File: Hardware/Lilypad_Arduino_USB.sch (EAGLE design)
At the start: 44 parts, among them U1 MCP73831, U2 MIC5219, U3 ATMEGA32U4QFN, X1 USB-MICROB, Y1 8MHz

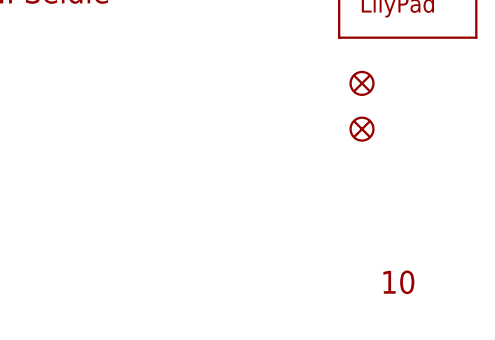
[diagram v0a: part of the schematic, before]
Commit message: Change micro USB connector to more robust package.
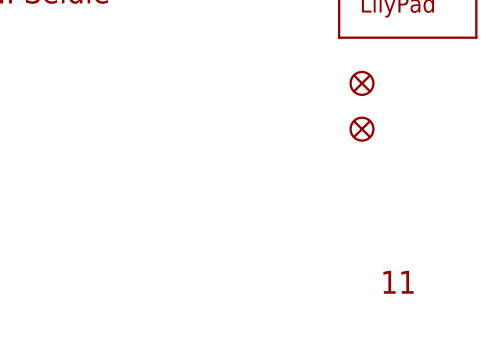
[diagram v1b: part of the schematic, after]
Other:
- note added: "11"
- note removed: "10"
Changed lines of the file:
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@@
 <layer number="144" name="Drill_legend" color="7" fill="1" visible="yes" active="yes"/>
 <layer number="151" name="HeatSink" color="7" fill="1" visible="yes" active="yes"/>
+<layer number="199" name="Contour" color="7" fill="1" visible="yes" active="yes"/>
 <layer number="200" name="200bmp" color="1" fill="10" visible="no" active="no"/>
 <layer number="201" name="201bmp" color="2" fill="1" visible="no" active="no"/>
@@
 <text x="45.72" y="120.65" size="1.27" layer="97">MIC5219 BYPASS</text>
 <text x="171.45" y="11.43" size="2.54" layer="94">Mike Hord</text>
-<text x="238.252" y="7.112" size="2.54" layer="94">10</text>
+<text x="238.252" y="7.112" size="2.54" layer="94">11</text>
 <text x="170.18" y="43.18" size="2.54" layer="94">Original Lilypad Design by:</text>
 <text x="170.18" y="39.37" size="2.54" layer="94">L. Buechly and N. Seidle</text>

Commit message: Changed version number in both files.
Masked via at .35, .275 to provide a test point for the charge circuit.
Add USR mask on the user control LED to make it more clear what it does.

Closes issues 1 and 2.
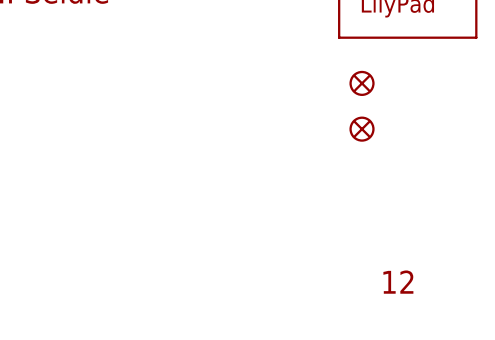
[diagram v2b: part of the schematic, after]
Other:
- note added: "12"
- note removed: "11"
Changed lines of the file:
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@@
 <text x="45.72" y="120.65" size="1.27" layer="97">MIC5219 BYPASS</text>
 <text x="171.45" y="11.43" size="2.54" layer="94">Mike Hord</text>
-<text x="238.252" y="7.112" size="2.54" layer="94">11</text>
+<text x="238.252" y="7.112" size="2.54" layer="94">12</text>
 <text x="170.18" y="43.18" size="2.54" layer="94">Original Lilypad Design by:</text>
 <text x="170.18" y="39.37" size="2.54" layer="94">L. Buechly and N. Seidle</text>

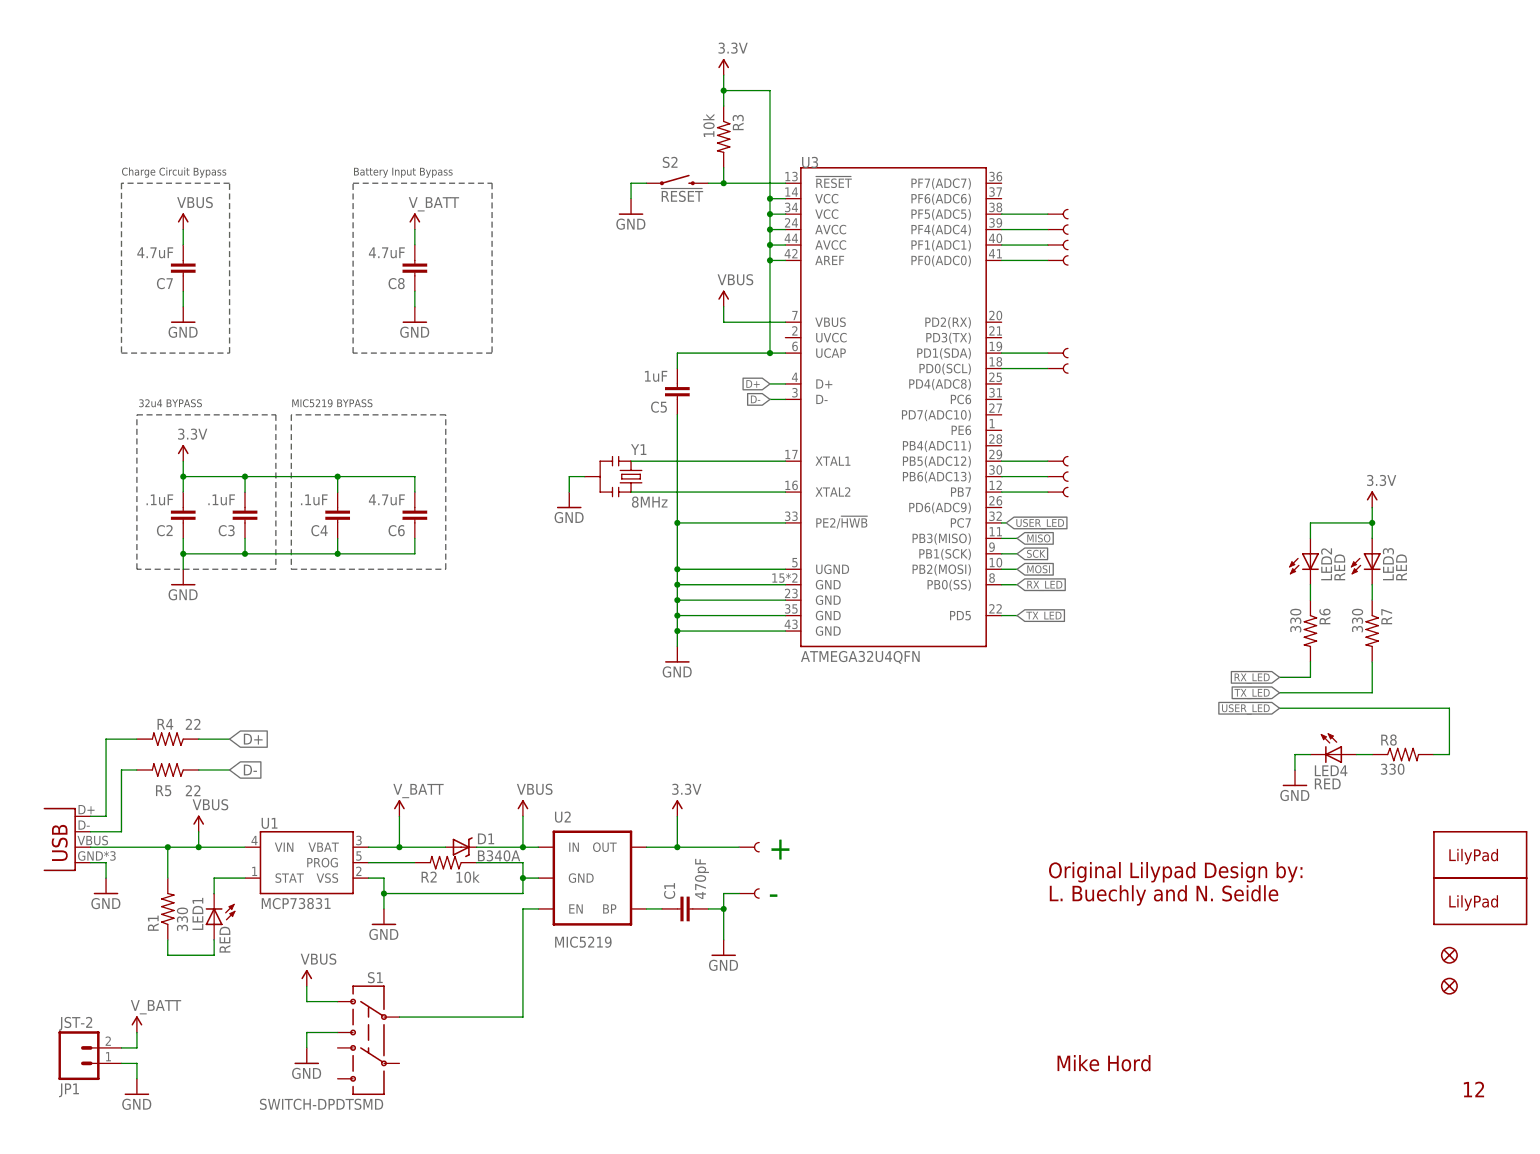
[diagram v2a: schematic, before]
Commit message: Quality Control Revision to PCB layout
Changed:
- Updated all 0402 footprints to 0603
- Updated with new 1:1 footprint of 32u4 IC
- Rerouted all traces straight away from IC
- Added trestrict under IC to mitigate gnd plane
- Moved crystal closer to IC
- Updated microUSB footprint for new production part
- Added test point for charge circuit
- Updated version number in bottom copper and schematic
- Added silk for charge and stat LEDs
- Added gnd vias to mitigate orphaned pours
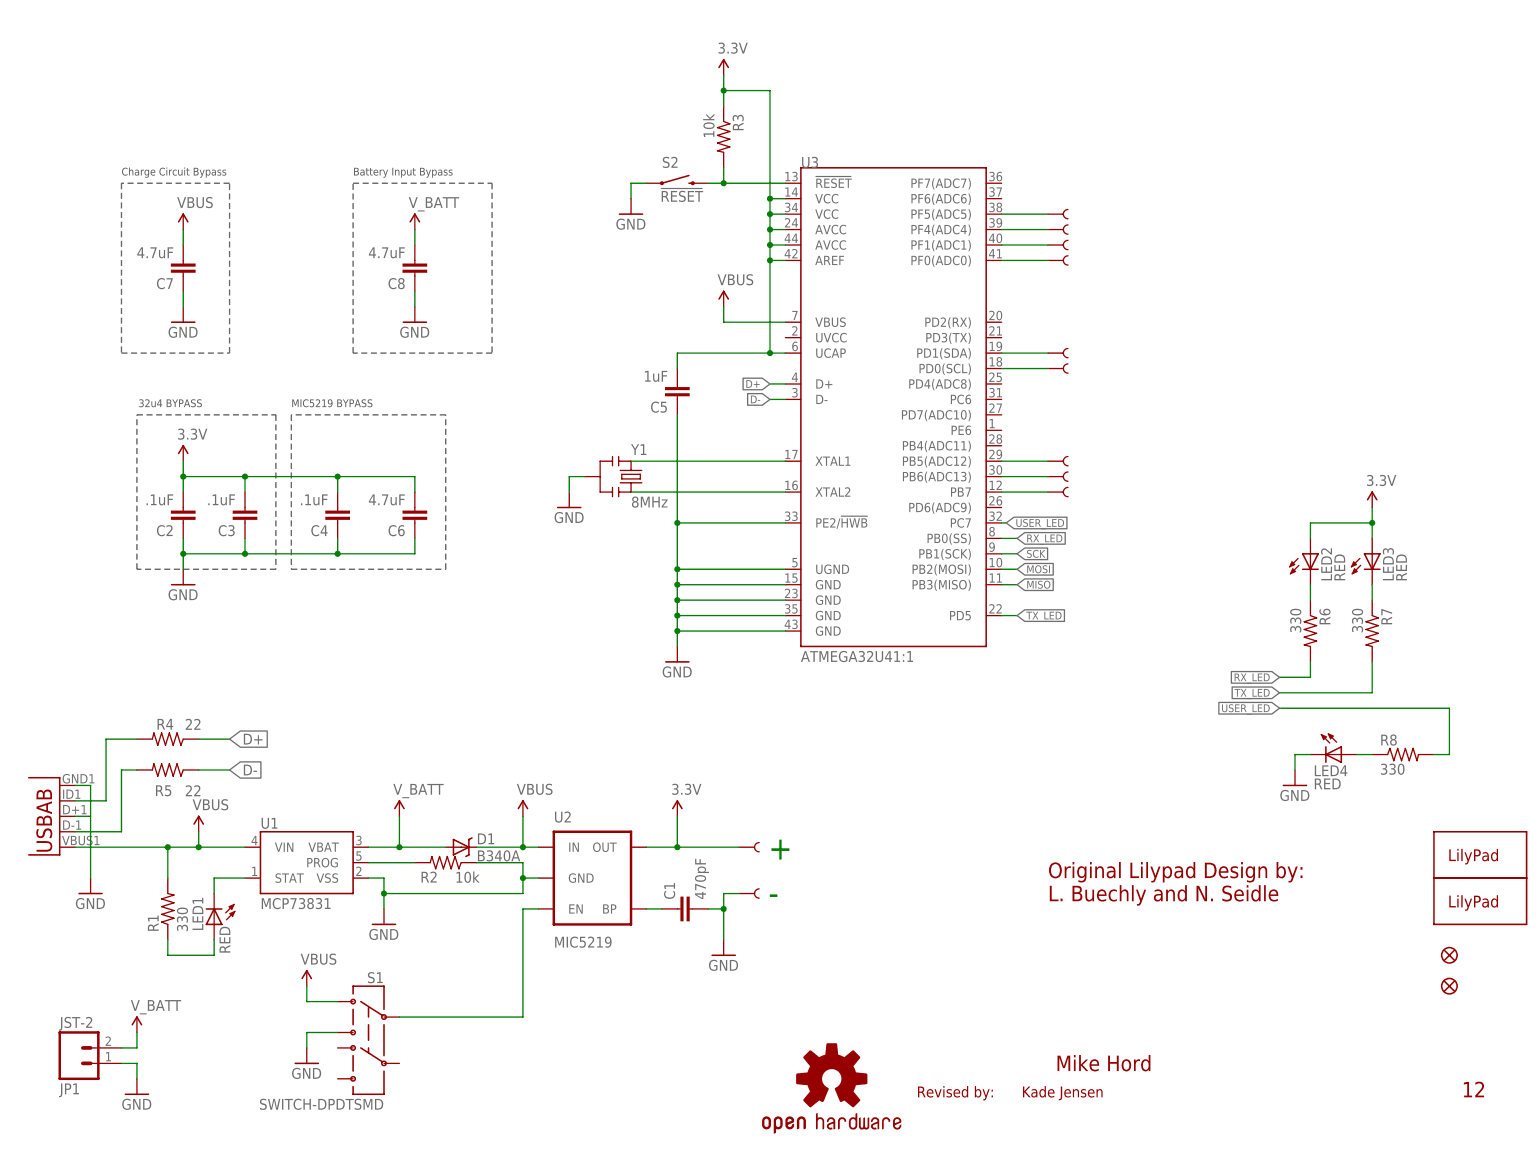
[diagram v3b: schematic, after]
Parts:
- added U$5: OSHW-LOGOM, SparkFun:OSHW-LOGOM
- JP2, JP3: value FIDUCIALUFIDUCIAL -> FIDUCIAL1X2; device SparkFun:FIDUCIALUFIDUCIAL -> SparkFun:FIDUCIAL1X2
- R2, R3, R4, R5, R6: device SparkFun-Passives:RESISTOR0603-RES -> SparkFun-Resistors:RESISTOR0603-RES
- U3: value ATMEGA32U4QFN -> ATMEGA32U41:1; device SparkFun-DigitalIC:ATMEGA32U4QFN -> Testing:ATMEGA32U41:1
- X1: value USB-MICROB -> (none); device SparkFun-Connectors:USB-MICROB -> Testing:USB-AB"""; PROD_ID CONN-09505 -> (none)
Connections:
- new net N$22: X1.D+
- net N$20: now also X1.USBID; no longer X1.D+
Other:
- note added: "Kade Jensen"
- note added: "Revised by:"
- moved on the sheet: U3
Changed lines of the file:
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@@
 <?xml version="1.0" encoding="utf-8"?>
 <!DOCTYPE eagle SYSTEM "eagle.dtd">
-<eagle version="6.3">
+<eagle version="6.4">
 <drawing>
 <settings>
@@
 <layer number="106" name="bPlate" color="7" fill="1" visible="yes" active="yes"/>
 <layer number="107" name="Crop" color="7" fill="1" visible="yes" active="yes"/>
+<layer number="108" name="tplace-old" color="10" fill="1" visible="yes" active="yes"/>
+<layer number="109" name="ref-old" color="11" fill="1" visible="yes" active="yes"/>
 <layer number="116" name="Patch_BOT" color="9" fill="4" visible="yes" active="yes"/>
 <layer number="121" name="_tsilk" color="7" fill="1" visible="yes" active="yes"/>
@@
 <attribute name="NO_PART" value="1"/>
 </part>
-<part name="U3" library="SparkFun-DigitalIC" deviceset="ATMEGA32U4" device="QFN">
+<part name="U3" library="Testing" deviceset="ATMEGA32U4" device="1:1">
 <attribute name="PROD_ID" value="IC-10828"/>
 </part>
@@
 <attribute name="PROD_ID" value="CONN-08352"/>
 </part>
-<part name="X1" library="SparkFun-Connectors" deviceset="USB" device="-MICROB">
-<attribute name="PROD_ID" value="CONN-09505"/>
-</part>
+<part name="X1" library="Testing" deviceset="USB-AB" device="&quot;&quot;&quot;"/>
 <part name="LED1" library="SparkFun-LED" deviceset="LED" device="0603" value="RED">
 <attribute name="PROD_ID" value="DIO-00819"/>
@@
 <part name="P+1" library="SparkFun-Aesthetics" deviceset="3.3V" device=""/>
 <part name="U$14" library="SparkFun-Aesthetics" deviceset="V_BATT" device=""/>
-<part name="R2" library="SparkFun-Passives" deviceset="RESISTOR" device="0603-RES" value="10k">
+<part name="R2" library="SparkFun-Resistors" deviceset="RESISTOR" device="0603-RES" value="10k">
 <attribute name="PROD_ID" value="RES-00824"/>
 </part>
 <part name="GND4" library="SparkFun-Aesthetics" deviceset="GND" device=""/>
 <part name="P+2" library="SparkFun-Aesthetics" deviceset="3.3V" device=""/>
-<part name="R3" library="SparkFun-Passives" deviceset="RESISTOR" device="0603-RES" value="10k">
+<part name="R3" library="SparkFun-Resistors" deviceset="RESISTOR" device="0603-RES" value="10k">
 <attribute name="PROD_ID" value="RES-00824"/>
 </part>
 <part name="GND5" library="SparkFun-Aesthetics" deviceset="GND" device=""/>
 <part name="U$16" library="SparkFun-Aesthetics" deviceset="5V" device="" value="VBUS"/>
-<part name="R4" library="SparkFun-Passives" deviceset="RESISTOR" device="0603-RES" value="22">
+<part name="R4" library="SparkFun-Resistors" deviceset="RESISTOR" device="0603-RES" value="22">
 <attribute name="PROD_ID" value="RES-08698"/>
 </part>
-<part name="R5" library="SparkFun-Passives" deviceset="RESISTOR" device="0603-RES" value="22">
+<part name="R5" library="SparkFun-Resistors" deviceset="RESISTOR" device="0603-RES" value="22">
 <attribute name="PROD_ID" value="RES-08698"/>
 </part>
 <part name="GND7" library="SparkFun-Aesthetics" deviceset="GND" device=""/>
-<part name="R6" library="SparkFun-Passives" deviceset="RESISTOR" device="0603-RES" value="330">
+<part name="R6" library="SparkFun-Resistors" deviceset="RESISTOR" device="0603-RES" value="330">
 <attribute name="PROD_ID" value="RES-00818"/>
 </part>
@@
 </part>
 <part name="GND10" library="SparkFun-Aesthetics" deviceset="GND" device=""/>
-<part name="JP2" library="SparkFun" deviceset="FIDUCIAL" device="UFIDUCIAL"/>
-<part name="JP3" library="SparkFun" deviceset="FIDUCIAL" device="UFIDUCIAL"/>
+<part name="JP2" library="SparkFun" deviceset="FIDUCIAL" device="1X2"/>
+<part name="JP3" library="SparkFun" deviceset="FIDUCIAL" device="1X2"/>
 <part name="D1" library="SparkFun-DiscreteSemi" deviceset="DIODE-SCHOTTKY" device="_" value="B340A">
 <attribute name="PROD_ID" value="DIO-09886"/>
@@
 <part name="U$1" library="LilyPad-Wearables" deviceset="LOGO-LP" device="LPA"/>
 <part name="GND12" library="SparkFun-Aesthetics" deviceset="GND" device=""/>
+<part name="U$5" library="SparkFun" deviceset="OSHW-LOGO" device="M"/>
 </parts>
 <sheets>
@@
 <text x="17.78" y="158.75" size="1.27" layer="97">Charge Circuit Bypass</text>
 <text x="55.88" y="158.75" size="1.27" layer="97">Battery Input Bypass</text>
+<text x="148.59" y="7.112" size="1.778" layer="94">Revised by:</text>
+<text x="165.862" y="7.112" size="1.778" layer="94">Kade Jensen</text>
 </plain>
 <instances>
@@
 <attribute name="PROD_ID" x="10.16" y="15.24" size="1.27" layer="96" rot="MR180" display="off"/>
 </instance>
-<instance part="X1" gate="G$1" x="10.16" y="45.72" rot="MR0">
-<attribute name="PROD_ID" x="10.16" y="45.72" size="1.27" layer="96" rot="MR0" display="off"/>
-</instance>
+<instance part="X1" gate="G$1" x="5.08" y="53.34" rot="MR0"/>
 <instance part="LED1" gate="G$1" x="33.02" y="35.56" smashed="yes" rot="R180">
 <attribute name="PROD_ID" x="33.02" y="35.56" size="1.27" layer="96" rot="R180" display="off"/>
@@
 <instance part="GND1" gate="1" x="48.26" y="12.7"/>
 <instance part="GND2" gate="1" x="60.96" y="35.56"/>
-<instance part="GND3" gate="1" x="15.24" y="40.64"/>
+<instance part="GND3" gate="1" x="12.7" y="40.64"/>
 <instance part="U$12" gate="G$1" x="30.48" y="50.8"/>
 <instance part="P+1" gate="G$1" x="109.22" y="53.34"/>
@@
 <instance part="U$1" gate="G$1" x="236.22" y="45.72"/>
 <instance part="GND12" gate="1" x="210.82" y="58.42"/>
+<instance part="U$5" gate="G$1" x="134.62" y="10.16"/>
 </instances>
 <busses>
@@
 <wire x1="83.82" y1="45.72" x2="83.82" y2="43.18" width="0.1524" layer="91"/>
 <junction x="83.82" y="43.18"/>
-</segment>
-<segment>
-<pinref part="X1" gate="G$1" pin="GND"/>
-<pinref part="GND3" gate="1" pin="GND"/>
-<wire x1="12.7" y1="45.72" x2="15.24" y2="45.72" width="0.1524" layer="91"/>
-<wire x1="15.24" y1="45.72" x2="15.24" y2="43.18" width="0.1524" layer="91"/>
 </segment>
 <segment>
@@
 <pinref part="LED4" gate="G$1" pin="C"/>
 <wire x1="210.82" y1="63.5" x2="213.36" y2="63.5" width="0.1524" layer="91"/>
+</segment>
+<segment>
+<pinref part="GND3" gate="1" pin="GND"/>
+<wire x1="12.7" y1="43.18" x2="12.7" y2="58.42" width="0.1524" layer="91"/>
+<pinref part="X1" gate="G$1" pin="GND"/>
+<wire x1="12.7" y1="58.42" x2="10.16" y2="58.42" width="0.1524" layer="91"/>
 </segment>
 </net>
@@
 <pinref part="X1" gate="G$1" pin="VBUS"/>
 <pinref part="U1" gate="G$1" pin="VIN"/>
-<wire x1="12.7" y1="48.26" x2="25.4" y2="48.26" width="0.1524" layer="91"/>
+<wire x1="10.16" y1="48.26" x2="25.4" y2="48.26" width="0.1524" layer="91"/>
 <pinref part="R1" gate="G$1" pin="2"/>
 <wire x1="25.4" y1="48.26" x2="30.48" y2="48.26" width="0.1524" layer="91"/>
@@
 <wire x1="17.78" y1="60.96" x2="17.78" y2="50.8" width="0.1524" layer="91"/>
 <pinref part="X1" gate="G$1" pin="D-"/>
-<wire x1="17.78" y1="50.8" x2="12.7" y2="50.8" width="0.1524" layer="91"/>
+<wire x1="17.78" y1="50.8" x2="10.16" y2="50.8" width="0.1524" layer="91"/>
 </segment>
 </net>
@@
 <pinref part="R4" gate="G$1" pin="2"/>
 <wire x1="20.32" y1="66.04" x2="15.24" y2="66.04" width="0.1524" layer="91"/>
-<wire x1="15.24" y1="66.04" x2="15.24" y2="53.34" width="0.1524" layer="91"/>
-<pinref part="X1" gate="G$1" pin="D+"/>
-<wire x1="15.24" y1="53.34" x2="12.7" y2="53.34" width="0.1524" layer="91"/>
+<pinref part="X1" gate="G$1" pin="USBID"/>
+<wire x1="10.16" y1="55.88" x2="15.24" y2="55.88" width="0.1524" layer="91"/>
+<wire x1="15.24" y1="55.88" x2="15.24" y2="66.04" width="0.1524" layer="91"/>
 </segment>
 </net>
@@
 <segment>
 <pinref part="U3" gate="G$1" pin="PB0(SS)"/>
-<wire x1="162.56" y1="91.44" x2="165.1" y2="91.44" width="0.1524" layer="91"/>
-<label x="165.1" y="91.44" size="1.27" layer="95" xref="yes"/>
+<wire x1="162.56" y1="99.06" x2="165.1" y2="99.06" width="0.1524" layer="91"/>
+<label x="165.1" y="99.06" size="1.27" layer="95" xref="yes"/>
 </segment>
 </net>
@@
 <segment>
 <pinref part="U3" gate="G$1" pin="PB3(MISO)"/>
-<wire x1="162.56" y1="99.06" x2="165.1" y2="99.06" width="0.1524" layer="91"/>
-<label x="165.1" y="99.06" size="1.27" layer="95" xref="yes"/>
+<wire x1="162.56" y1="91.44" x2="165.1" y2="91.44" width="0.1524" layer="91"/>
+<label x="165.1" y="91.44" size="1.27" layer="95" xref="yes"/>
 </segment>
 </net>
@@
 </segment>
 </net>
+<net name="N$22" class="0">
+<segment>
+<pinref part="X1" gate="G$1" pin="D+"/>
+<wire x1="10.16" y1="53.34" x2="12.7" y2="53.34" width="0.1524" layer="91"/>
+</segment>
+</net>

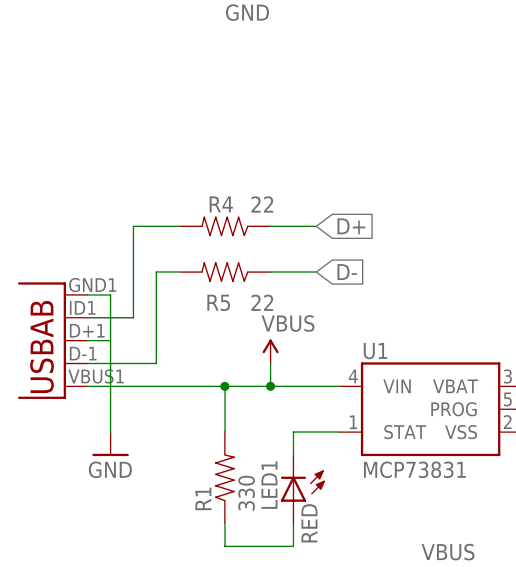
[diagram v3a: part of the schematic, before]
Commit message: Fixing D+ trace connection
ID line on USB connector was routed to D+ on micro and D+ on USB
connector was unrouted. Fixed now.
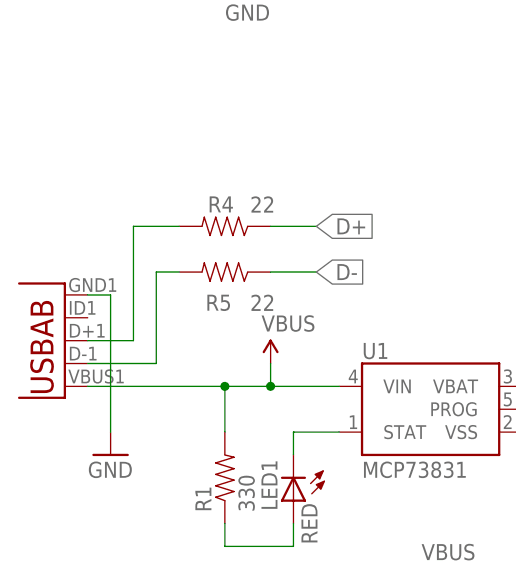
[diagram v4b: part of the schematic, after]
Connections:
- removed net N$22: X1.D+
- net N$20: now also X1.D+; no longer X1.USBID
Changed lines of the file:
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@@
 <pinref part="R4" gate="G$1" pin="2"/>
 <wire x1="20.32" y1="66.04" x2="15.24" y2="66.04" width="0.1524" layer="91"/>
-<pinref part="X1" gate="G$1" pin="USBID"/>
-<wire x1="10.16" y1="55.88" x2="15.24" y2="55.88" width="0.1524" layer="91"/>
-<wire x1="15.24" y1="55.88" x2="15.24" y2="66.04" width="0.1524" layer="91"/>
+<wire x1="15.24" y1="53.34" x2="15.24" y2="66.04" width="0.1524" layer="91"/>
+<pinref part="X1" gate="G$1" pin="D+"/>
+<wire x1="10.16" y1="53.34" x2="15.24" y2="53.34" width="0.1524" layer="91"/>
 </segment>
 </net>
@@
 </segment>
 </net>
-<net name="N$22" class="0">
-<segment>
-<pinref part="X1" gate="G$1" pin="D+"/>
-<wire x1="10.16" y1="53.34" x2="12.7" y2="53.34" width="0.1524" layer="91"/>
-</segment>
-</net>
